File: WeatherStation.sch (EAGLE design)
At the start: 9 parts, among them J1 EDISON_CONNECTOR_FULLMOUNTING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, J2 EDISON_CONNECTOR_FULLHEADER

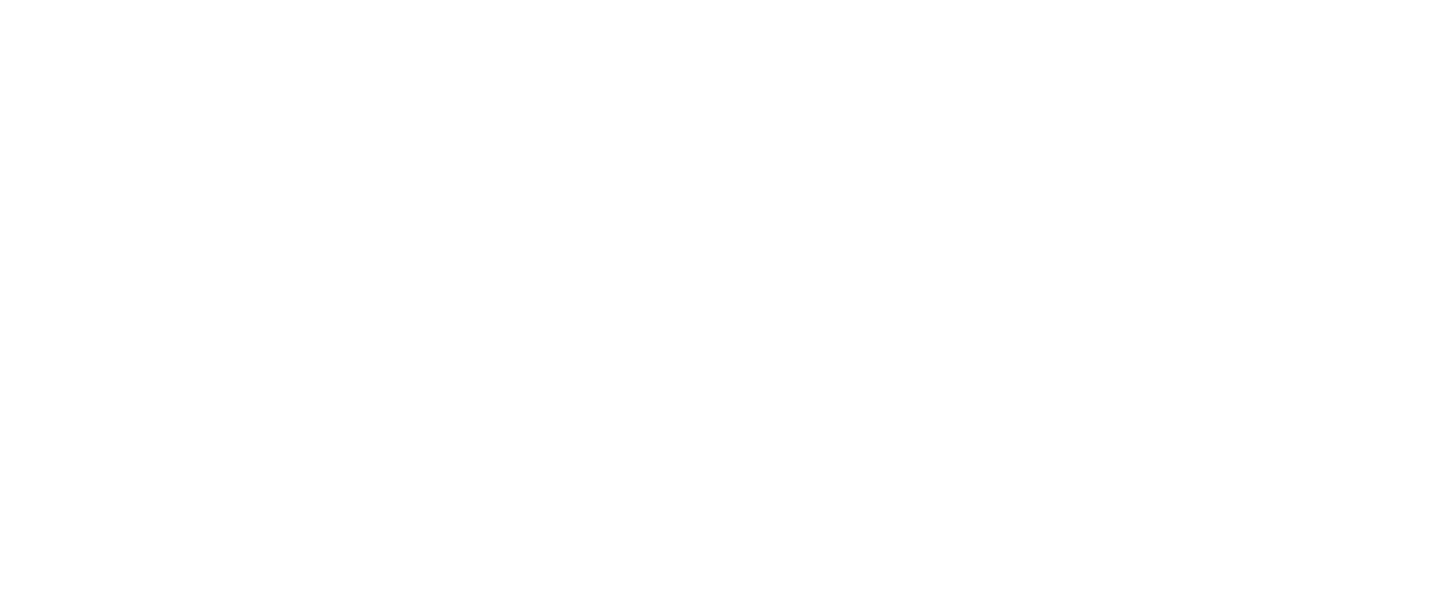
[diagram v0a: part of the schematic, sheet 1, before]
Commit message: added MCP73831 circuit
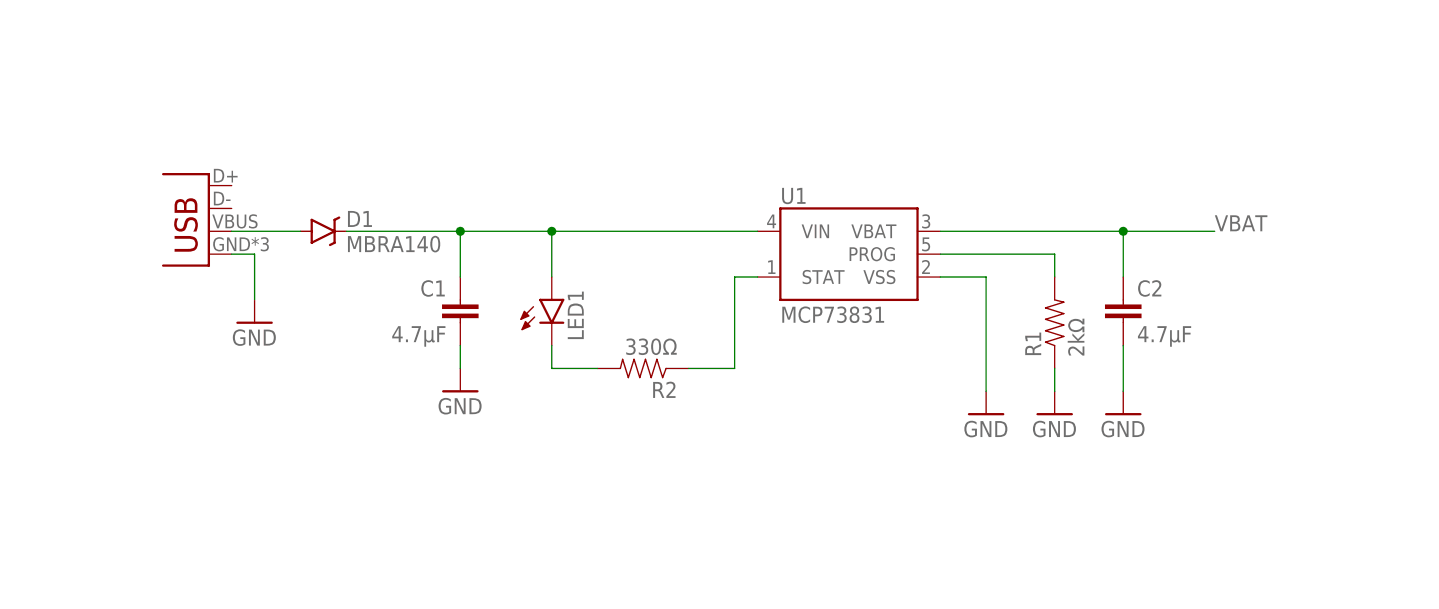
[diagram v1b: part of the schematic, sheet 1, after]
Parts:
- added C1, C2: 4.7µF, SparkFun-Capacitors:CAP0805
- added D1: MBRA140, SparkFun-DiscreteSemi:MBRA140
- added JP1: USB-MICROB, SparkFun-Connectors:USB-MICROB
- added LED1: (no value), SparkFun-LED:LED0603
- added R1: 2kΩ, SparkFun-Resistors:RESISTOR0603-RES
- added R2: 330Ω, SparkFun-Resistors:RESISTOR0603-RES
- added U1: MCP73831, SparkFun-PowerIC:MCP73831
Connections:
- new net N$1: D1.A, JP1.VBUS
- new net N$2: C1.1, D1.C, LED1.A, U1.VIN
- new net N$4: LED1.C, R2.2
- new net N$5: R2.1, U1.STAT
- new net N$6: R1.2, U1.PROG
- new net VBAT: C2.1, U1.VBAT
- net GND: now also C1.2, C2.2, JP1.GND, R1.1, U1.VSS
